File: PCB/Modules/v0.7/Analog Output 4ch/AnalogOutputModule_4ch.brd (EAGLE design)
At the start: 85 x 85 mm, 40 parts, among them IC1 SN65HVD31DR, IC2 SN65HVD31DR, IC3 AD5754RBREZ, IC4 REF193GSZ

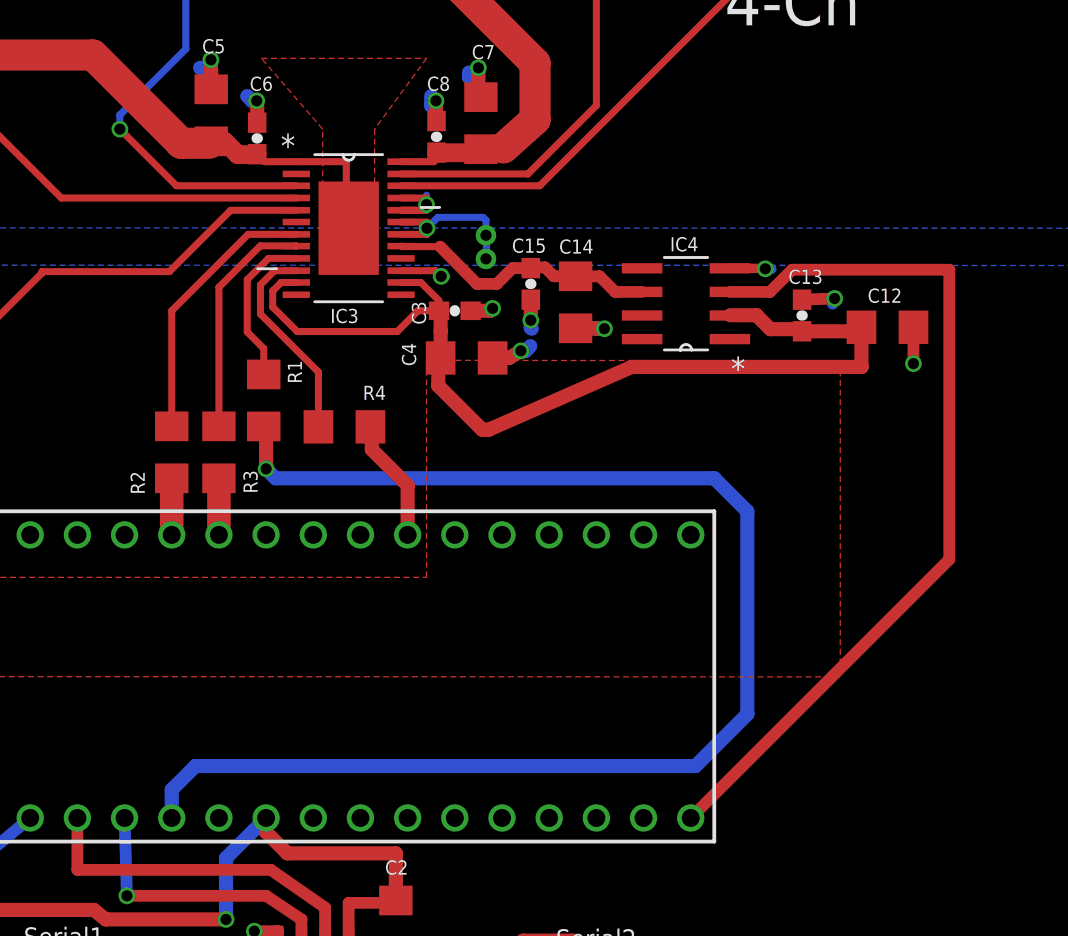
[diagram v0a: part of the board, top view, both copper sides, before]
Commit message: -Improved Analog Output Module schematic organization and labeling -Thickened trace connecting Analog Output Module ground planes
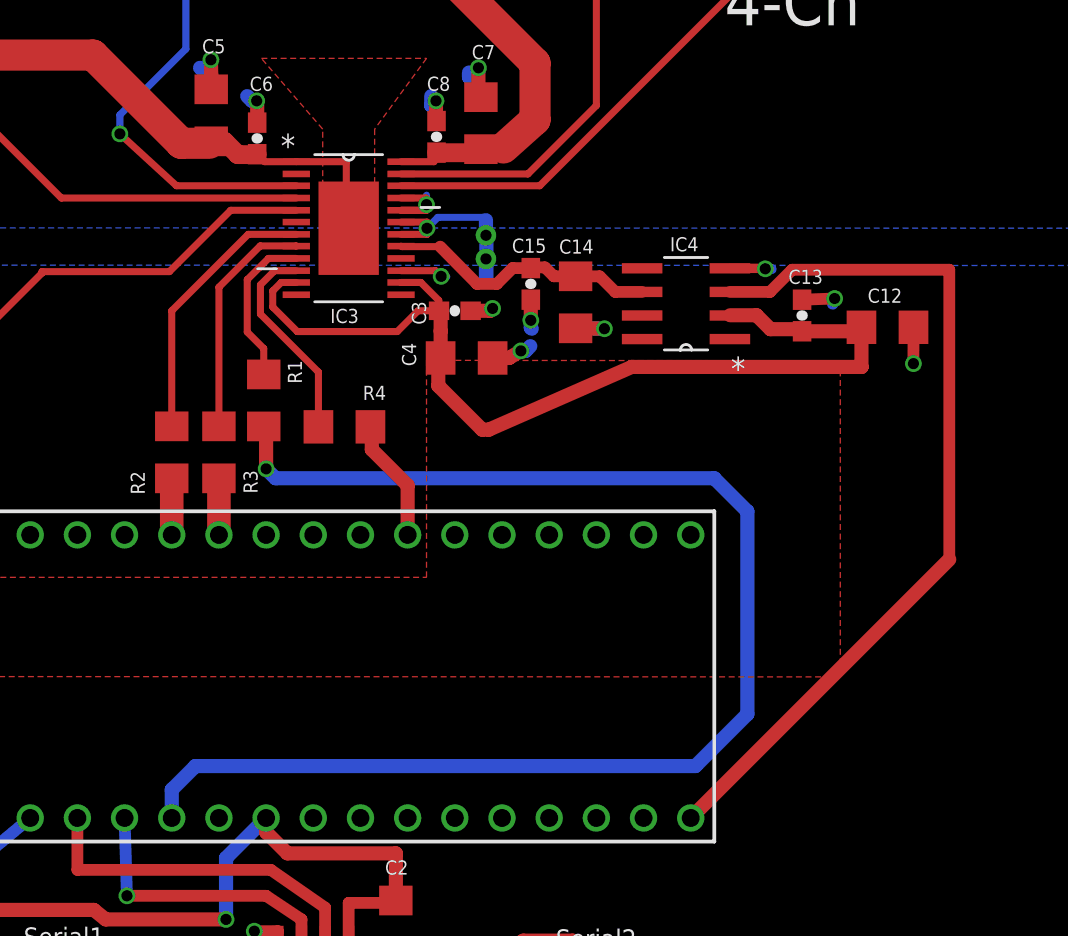
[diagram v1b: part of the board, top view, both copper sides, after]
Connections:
- net N$20 renamed REF_ENABLE
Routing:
- net GND: track 29.7 -> 31.8 mm
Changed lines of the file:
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@@
 <wire x1="47.5234" y1="49.4792" x2="47.8028" y2="49.4792" width="0.381" layer="16"/>
 <wire x1="47.8028" y1="49.4792" x2="47.8282" y2="49.4538" width="0.381" layer="16"/>
-<wire x1="49.9618" y1="50.1142" x2="49.9618" y2="51.7652" width="0.381" layer="16"/>
+<wire x1="49.9618" y1="50.1142" x2="49.9618" y2="51.7652" width="0.762" layer="16"/>
 <contactref element="IC4" pad="4"/>
 <wire x1="63.0682" y1="49.911" x2="64.9478" y2="49.911" width="0.508" layer="1"/>
@@
 <wire x1="52.3494" y1="47.117" x2="52.3494" y2="46.7106" width="0.762" layer="16"/>
 <wire x1="52.3494" y1="46.7106" x2="52.4002" y2="46.6598" width="0.762" layer="16"/>
-<wire x1="49.9364" y1="50.419" x2="49.9618" y2="50.1142" width="0" layer="19" extent="16-16"/>
+<wire x1="49.9618" y1="50.1142" x2="49.9618" y2="49.2506" width="0.762" layer="16"/>
+<wire x1="49.9618" y1="49.2506" x2="49.9364" y2="49.2252" width="0.762" layer="16"/>
+<wire x1="49.9364" y1="49.2252" x2="49.9364" y2="50.419" width="0.762" layer="16"/>
 </signal>
 <signal name="AGND">
@@
 <wire x1="45.3644" y1="51.7398" x2="46.7614" y2="51.7398" width="0.381" layer="1"/>
 <wire x1="46.7614" y1="51.7398" x2="46.7614" y2="52.07" width="0.381" layer="1"/>
-<wire x1="49.9364" y1="51.689" x2="49.9364" y2="52.5018" width="0.381" layer="16"/>
+<wire x1="49.9364" y1="51.689" x2="49.9364" y2="52.5018" width="0.762" layer="16"/>
 <wire x1="49.9364" y1="52.5018" x2="49.784" y2="52.6542" width="0.381" layer="16"/>
 <wire x1="49.784" y1="52.6542" x2="47.3456" y2="52.6542" width="0.381" layer="16"/>
@@
 <contactref element="BNC3" pad="S"/>
 <wire x1="39.7256" y1="54.356" x2="33.274" y2="54.356" width="0.381" layer="1"/>
-<wire x1="33.274" y1="54.356" x2="30.226" y2="57.404" width="0.381" layer="1"/>
-<via x="30.226" y="57.404" extent="1-16" drill="0.6"/>
-<wire x1="30.226" y1="57.404" x2="30.226" y2="58.166" width="0.381" layer="16"/>
+<wire x1="33.274" y1="54.356" x2="30.226" y2="57.15" width="0.381" layer="1"/>
+<via x="30.226" y="57.15" extent="1-16" drill="0.6"/>
+<wire x1="30.226" y1="57.15" x2="30.226" y2="58.166" width="0.381" layer="16"/>
 <wire x1="30.226" y1="58.166" x2="33.782" y2="61.722" width="0.381" layer="16"/>
 <wire x1="33.782" y1="61.722" x2="33.782" y2="74.168" width="0.381" layer="16"/>
@@
 <wire x1="45.4152" y1="51.0794" x2="45.3644" y2="51.1048" width="0.381" layer="1"/>
 </signal>
-<signal name="N$20">
+<signal name="REF_ENABLE">
 <contactref element="IC4" pad="3"/>
-<contactref element="U$1" pad="32/A13"/>
-<wire x1="60.96" y1="20.32" x2="74.8792" y2="34.2392" width="0.635" layer="1"/>
 <wire x1="74.8792" y1="34.2392" x2="74.8792" y2="49.8348" width="0.635" layer="1"/>
 <wire x1="74.8792" y1="49.8348" x2="66.421" y2="49.8348" width="0.635" layer="1"/>
 <wire x1="66.421" y1="49.8348" x2="65.2272" y2="48.641" width="0.635" layer="1"/>
 <wire x1="65.2272" y1="48.641" x2="63.0682" y2="48.641" width="0.635" layer="1"/>
+<contactref element="U$1" pad="32/A13"/>
+<wire x1="60.96" y1="20.32" x2="74.8792" y2="34.2392" width="0.762" layer="1"/>
 </signal>
 <signal name="N$19">
